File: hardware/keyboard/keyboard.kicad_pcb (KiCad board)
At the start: 2 copper layers, 234.9 x 95.7 mm, 81 parts, among them J1 Conn_01x02_Female, J2 Conn_01x03_Female, Q1 Q_NMOS_SGD, SW1 SW_Push, U1 SC0915, U10 CherryMX_LED, U11 CherryMX_LED, U12 CherryMX_LED, U13 CherryMX_LED, U14 CherryMX_LED, U15 CherryMX_LED, U16 CherryMX_LED, U17 CherryMX_LED, U18 CherryMX_LED, U19 CherryMX_LED, U2 MCP23008-xP, U20 CherryMX_LED, U21 CherryMX_LED, U22 CherryMX_LED, U23 CherryMX_LED, U24 CherryMX_LED, U25 CherryMX_LED, U26 CherryMX_LED, U27 CherryMX_LED, U28 CherryMX_LED, U29 CherryMX_LED, U3 CherryMX_LED, U30 CherryMX_LED, U31 CherryMX_LED, U32 CherryMX_LED, U33 CherryMX_LED, U34 CherryMX_LED, U35 CherryMX_LED, U36 CherryMX_LED, U4 CherryMX_LED, U5 CherryMX_LED, U6 CherryMX_LED, U7 CherryMX_LED, U8 CherryMX_LED, U9 CherryMX_LED

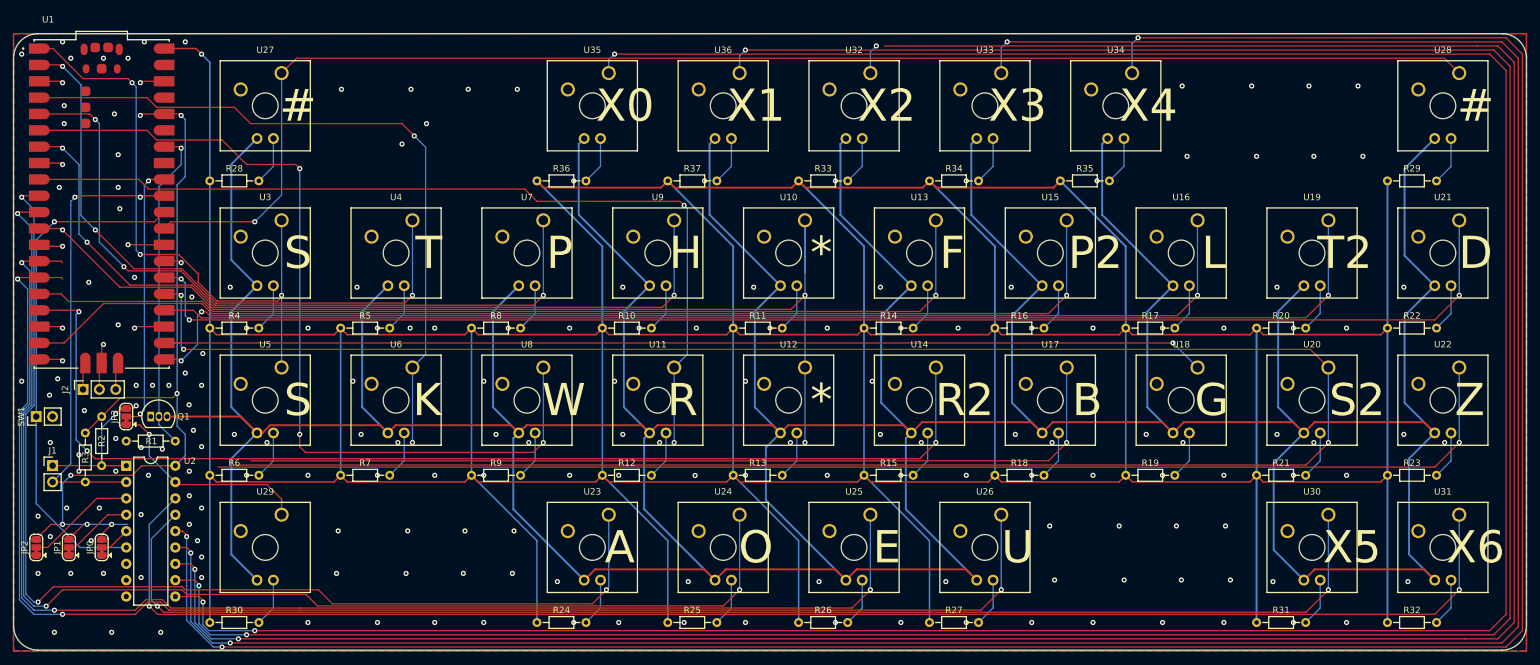
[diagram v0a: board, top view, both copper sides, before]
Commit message: Add documentation to PCB
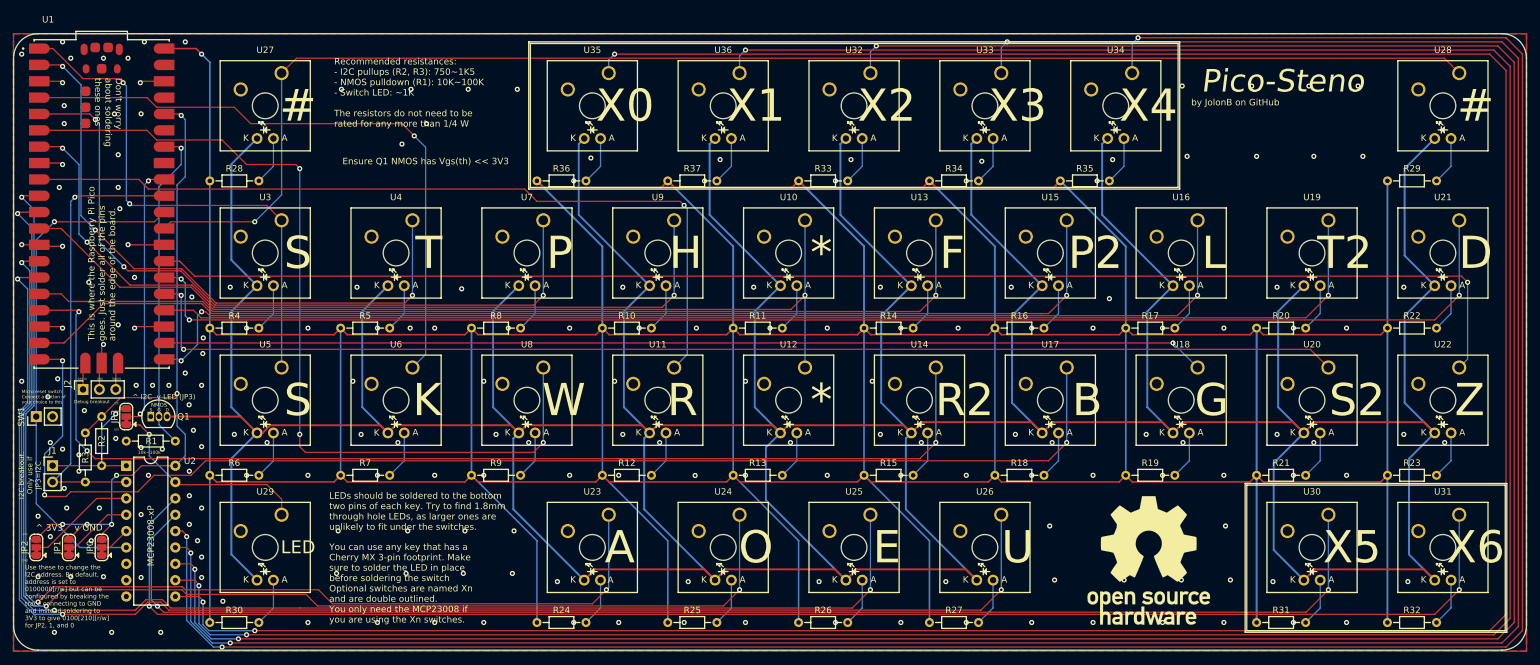
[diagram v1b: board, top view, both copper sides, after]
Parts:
- added REF**: OSHW-Logo_19x20mm_SilkScreen, Symbol:OSHW-Logo_19x20mm_SilkScreen, F.Cu at (252.5, 215.1)
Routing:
- net /KEY_S2: track 373.2 -> 190.2 mm, vias 3 -> 2
- net /KEY_B: track 143.3 -> 199.7 mm, vias 2 -> 3
- net /KEY_STAR: track 167.7 -> 147.9 mm, vias 3 -> 1
- net +3V3: track 126.6 -> 112.9 mm, vias 7 -> 6
- net /KEY_R: track 139.7 -> 128.0 mm, vias 2 -> 1
- net /KEY_K: track 109.9 -> 98.2 mm, vias 2 -> 1
- net /KEY_S: track 92.9 -> 82.0 mm, vias 3 -> 2
- net /KEY_Z: track 208.7 -> 217.6 mm, vias 2 -> 1
- net /KEY_U: track 225.8 -> 222.1 mm
- net /KEY_E: track 206.3 -> 202.6 mm
- net /KEY_G: track 164.5 -> 162.1 mm
- net GND: track 37.7 -> 40.1 mm, vias 194 -> 206
- net /I2C_SCL: track 24.1 -> 22.4 mm, vias 2 -> 1
- net /KEY_EXT2: track 409.2 -> 410.5 mm
- net /I2C_SDA: track 72.0 -> 71.0 mm, vias 2 -> 1
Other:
- board text added: "10k~100k"
- board text added: "3V3"
- board text added: "D"
- board text added: "Debug breakout"
- board text added: "Don't worry about soldering these ones"
- board text added: "Ensure Q1 NMOS has Vgs(th) << 3V3"
- board text added: "G"
- board text added: "GND"
- board text added: "I2C"
- board text added: "I2C breakout. Only use if JP3=I2C"
- board text added: "LED"
- board text added: "LEDs should be soldered to the bottom two pins of each key. Try to find 1.8mm through hole LEDs, as larger ones are unlikely to fit under the switches."
- board text added: "Micro reset switch Connect a button of your choice to this"
- board text added: "NMOS"
- board text added: "Pico-Steno"
- board text added: "Recommended resistances: - I2C pullups (R2, R3): 750~1K5 - NMOS pulldown (R1): 10K~100K - Switch LED: ~1K The resistors do not need to be rated for any more than 1/4 W"
- board text added: "S"
- board text added: "SWCLK"
- board text added: "SWDIO"
- board text added: "This is where the Raspberry Pi Pico goes. Just solder all of the pins around the edge of the board."
- board text added: "Use these to change the I2C address. By default, address is set to 0100000[r/w] but can be configured by breaking the trace connecting to GND and instead soldering to 3V3 to give 0100[210][r/w] for JP2, 1, and 0"
- board text added: "You can use any key that has a Cherry MX 3-pin footprint. Make sure to solder the LED in place before soldering the switch Optional switches are named Xn and are double outlined. You only need the MCP23008 if you are using the Xn switches."
- board text added: "^ 3V3 v GND"
- board text added: "^ I2C v LED (JP3)"
- board text added: "by JolonB on GitHub"
